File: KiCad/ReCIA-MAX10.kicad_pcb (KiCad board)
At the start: 4 copper layers, 17.4 x 51.4 mm, 9 parts, among them U1 AMS1117-3.3, U2 10M02SCU169, U5 8520_DIP

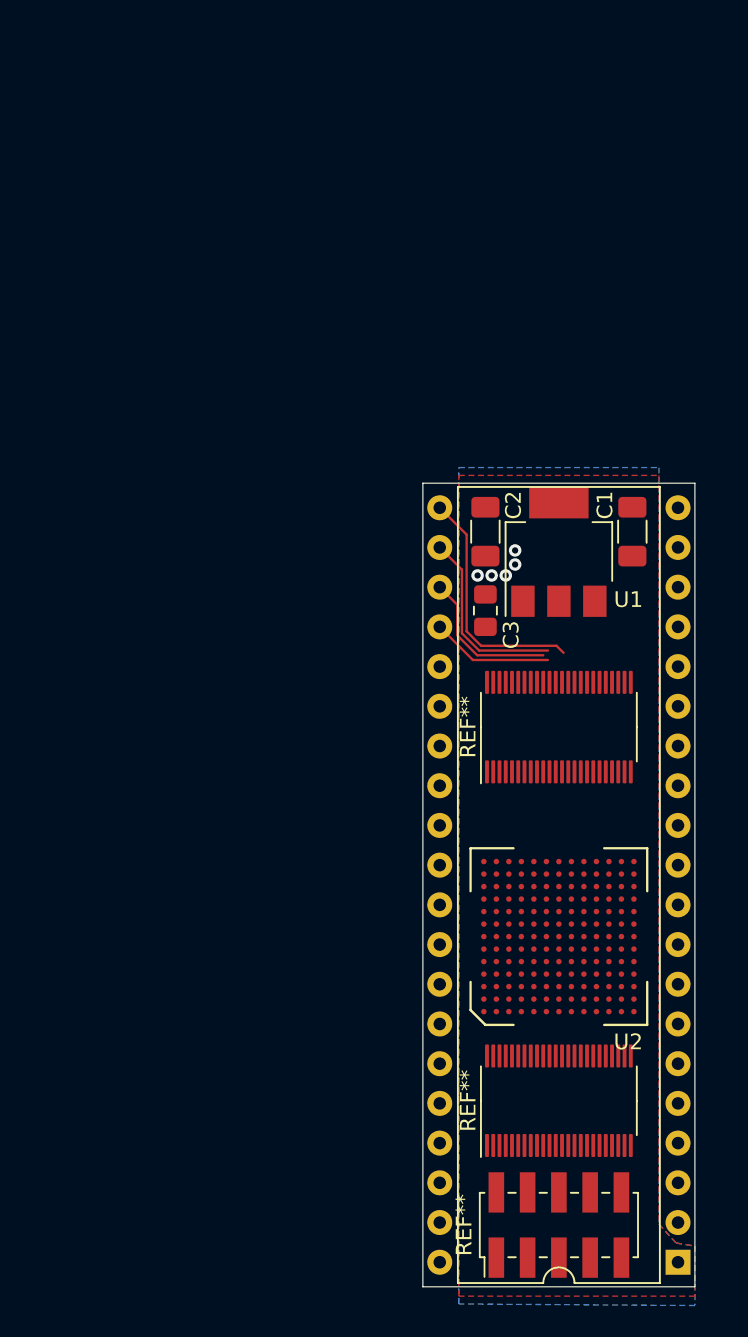
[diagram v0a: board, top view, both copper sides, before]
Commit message: Add FET bus-switch level shifters SN74CBT16210
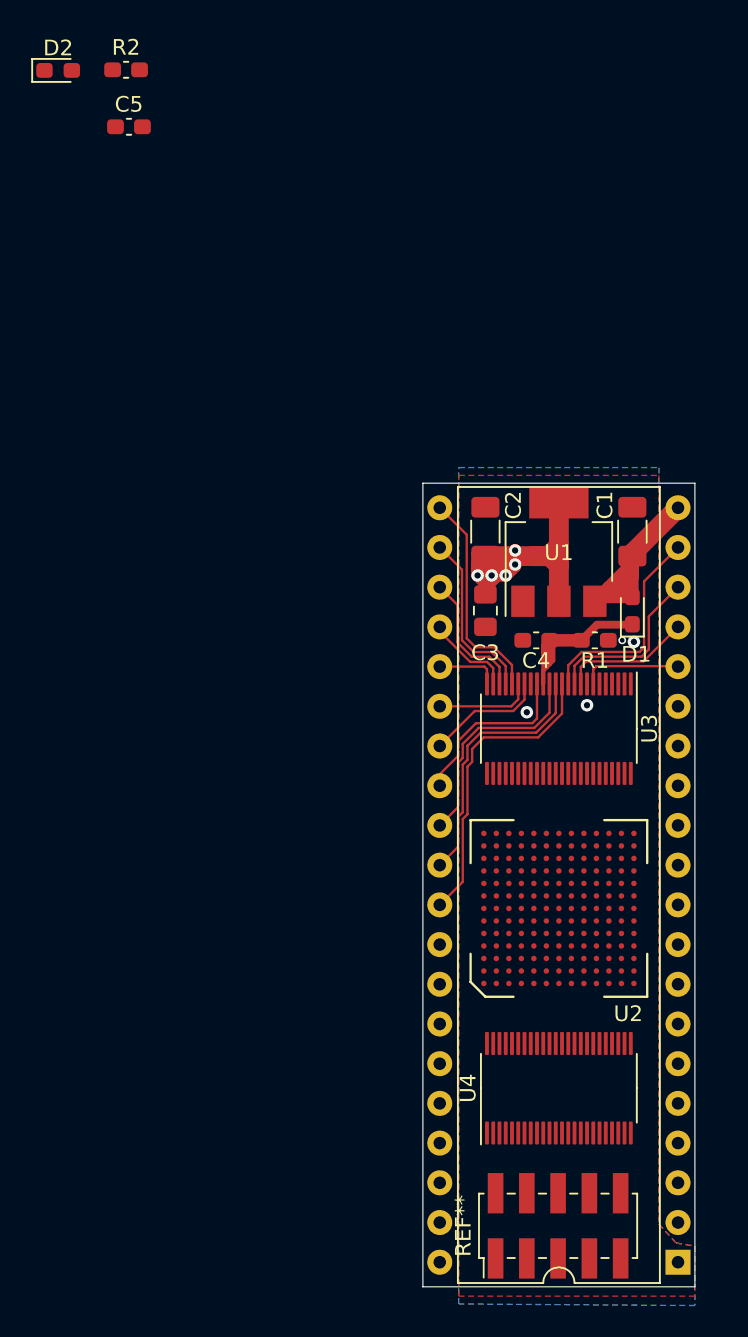
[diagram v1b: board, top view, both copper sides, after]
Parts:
- removed the REF** at (132.0, 96.8)
- removed the REF** at (132.0, 72.9)
- added C4: 0.1uF, Capacitor_SMD:C_0603_1608Metric_Pad1.08x0.95mm_HandSolder, F.Cu at (130.6, 67.3)
- added C5: 0.1uF, Capacitor_SMD:C_0603_1608Metric_Pad1.08x0.95mm_HandSolder, F.Cu at (104.5, 34.5)
- added D1: D_Small, Diode_SMD:D_0603_1608Metric_Pad1.05x0.95mm_HandSolder, F.Cu at (136.7, 65.5)
- added D2: D_Small, Diode_SMD:D_0603_1608Metric_Pad1.05x0.95mm_HandSolder, F.Cu at (100.0, 30.9)
- added R1: 2.9k, Capacitor_SMD:C_0603_1608Metric_Pad1.08x0.95mm_HandSolder, F.Cu at (134.3, 67.3)
- added R2: 2.9k, Capacitor_SMD:C_0603_1608Metric_Pad1.08x0.95mm_HandSolder, F.Cu at (104.3, 30.9)
- added U3: SN74CBT16210, Package_SO:TSSOP-48_4.4x9.7mm_P0.4mm, F.Cu at (132.0, 73.0)
- added U4: SN74CBT16210, Package_SO:TSSOP-48_4.4x9.7mm_P0.4mm, F.Cu at (132.0, 96.0)
- U5: value 8520_DIP -> 8520_DIP_SOCKET
- moved U2 1.80 mm to (132.0, 84.5)
- moved REF** 0.07 mm to (131.9, 104.8)
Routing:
- net 3V3: track 0.00 -> 33.3 mm
- net D2: track 0.00 -> 19.4 mm
- net D3: track 0.00 -> 16.7 mm
- net /4V3_U3: track 0.00 -> 16.7 mm
- net VCC: track 0.00 -> 16.4 mm
- net D4: track 0.00 -> 14.0 mm
- net TOD: track 0.00 -> 13.8 mm
- net D5: track 0.00 -> 11.2 mm
- net PC: track 0.00 -> 11.1 mm
- net PB7: track 0.00 -> 8.37 mm
- net D6: track 0.00 -> 7.66 mm
- net PB6: track 0.00 -> 6.45 mm
- net D7: track 0.00 -> 6.19 mm
- net E-CLK: track 0.00 -> 4.03 mm
- net FLAG: track 7.79 -> 5.69 mm
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
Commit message: Add JTAG-header
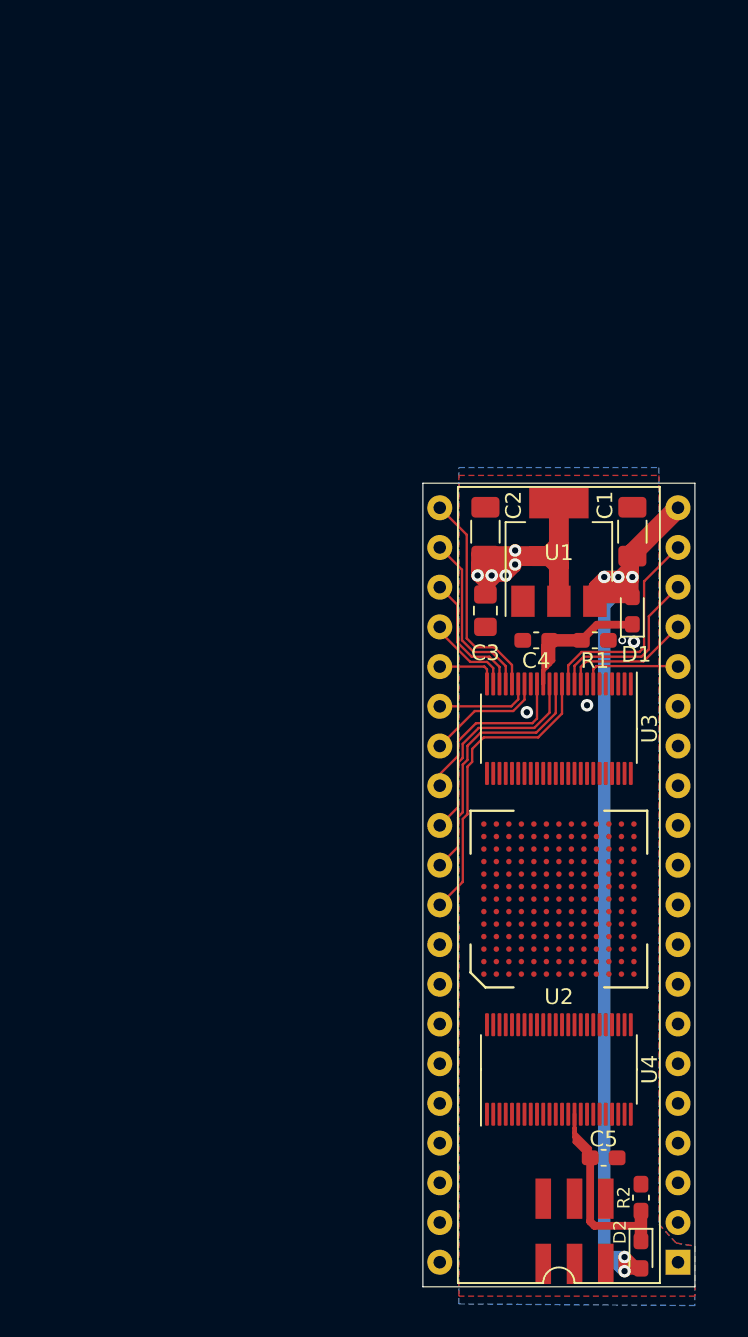
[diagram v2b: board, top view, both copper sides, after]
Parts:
- removed REF**: PinHeader_2x05_P2.00mm_Vertical_SMD, Connector_PinHeader_2.00mm:PinHeader_2x05_P2.00mm_Vertical_SMD
- added J1: Conn_02x03_Odd_Even, Connector_PinHeader_2.00mm:PinHeader_2x03_P2.00mm_Vertical_SMD, F.Cu at (133.0, 105.2)
- moved D2 84.4 mm to (137.2, 106.7), turned to 270 degrees
- moved R2 79.3 mm to (137.2, 103.0), turned to 90 degrees
- moved C5 72.6 mm to (134.9, 100.5)
- moved U4 1.20 mm to (132.0, 94.8)
- moved U2 0.60 mm to (132.0, 83.9)
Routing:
- net VCC: track 16.4 -> 75.6 mm, vias 0 -> 6
- net /4V3_U3: track 16.7 -> 33.8 mm
- net GND: track 0.00 -> 0.27 mm, vias 4 -> 3

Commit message: more routing and pin assignment
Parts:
- turned U4 to 180 degrees
- renumbered U3 to U2, U4 to U3, U2 to U4
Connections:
- net D2_3V3 renamed PB0_3V3
- C4 pad 1: /4V3_U3 -> /4V3_U2
- D1 pad 1: /4V3_U3 -> /4V3_U2
- R1 pad 1: /4V3_U3 -> /4V3_U2
- U2 pad 10: PC -> PB2
- U2 pad 11: TOD -> PB1
- U2 pad 12: D2 -> PB0
- U2 pad 15: /4V3_U3 -> /4V3_U2
- U2 pad 2: PB1 -> PB6
- U2 pad 3: PB2 -> PB7
- U2 pad 37: TOD_3V3 -> PB1_3V3
- U2 pad 38: PC_3V3 -> PB2_3V3
- U2 pad 39: PB7_3V3 -> PB3_3V3
- U2 pad 4: PB3 -> PC
- U2 pad 40: PB6_3V3 -> PB4_3V3
- U2 pad 43: PB4_3V3 -> TOD_3V3
- U2 pad 44: PB3_3V3 -> PC_3V3
- U2 pad 45: PB2_3V3 -> PB7_3V3
- U2 pad 46: PB1_3V3 -> PB6_3V3
- U2 pad 5: PB4 -> TOD
- U2 pad 7: PB6 -> PB4
- U2 pad 9: PB7 -> PB3
- U3 pad 16: Net-(U4-Pad16) -> PA7
- U3 pad 17: Net-(U4-Pad17) -> GND
- U3 pad 18: Net-(U4-Pad18) -> PA6
- U3 pad 19: Net-(U4-Pad19) -> PA5
- U3 pad 20: Net-(U4-Pad20) -> PA4
- U3 pad 21: Net-(U4-Pad21) -> PA3
- U3 pad 22: Net-(U4-Pad22) -> PA0
- U3 pad 23: Net-(U4-Pad23) -> PA1
- U3 pad 24: Net-(U4-Pad24) -> PA2
- U3 pad 32: Net-(U4-Pad32) -> GND
- U3 pad 41: Net-(U4-Pad41) -> GND
- U3 pad 8: Net-(U4-Pad8) -> GND
- U4 pad E10: 3V3 -> Net-(U4-PadE10)
- U4 pad E13: Net-(U2-PadE13) -> GND
- U4 pad F13: Net-(U2-PadF13) -> E-CLK_3V3
- U4 pad K13: Net-(U2-PadK13) -> FLAG_3V3
- U4 pad L13: Net-(U2-PadL13) -> CS_3V3
- U4 pad M13: Net-(U2-PadM13) -> RW_3V3
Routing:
- net D2: track 19.4 -> 0.00 mm
- net PB0: track 0.00 -> 18.6 mm
- net /4V3_U3: track 33.8 -> 15.9 mm
- net /4V3_U2: track 0.00 -> 16.7 mm
- net PB1: track 0.00 -> 15.8 mm
- net GND: track 0.27 -> 14.7 mm, vias 3 -> 28
- net PA7: track 0.00 -> 14.1 mm
- net PB2: track 0.00 -> 13.1 mm
- net PA6: track 0.00 -> 10.6 mm
- net PB3: track 0.00 -> 10.4 mm
- net E-CLK_3V3: track 0.00 -> 10.0 mm
- net PA0: track 0.00 -> 8.51 mm
- net PA5: track 0.00 -> 8.01 mm
- net PB4: track 0.00 -> 7.66 mm
- net FLAG_3V3: track 0.00 -> 6.76 mm
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
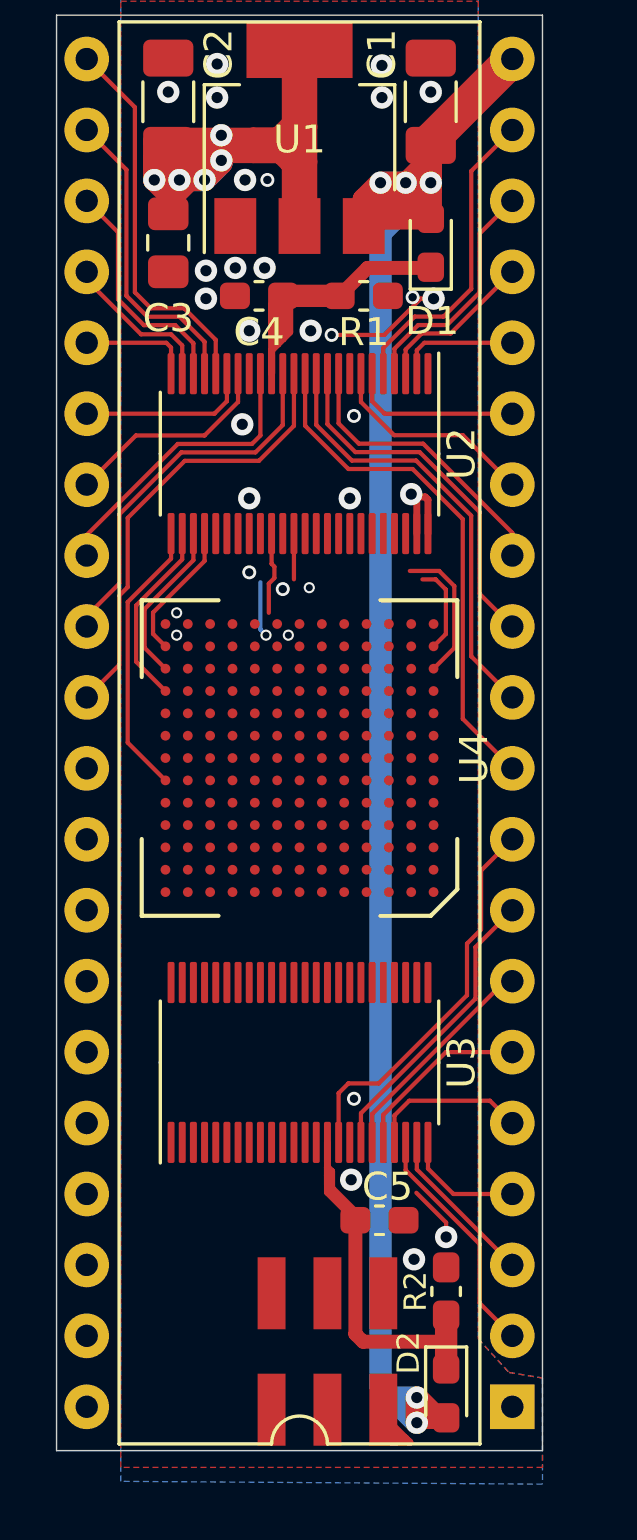
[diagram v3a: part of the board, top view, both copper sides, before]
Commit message: more routing and pin assignment
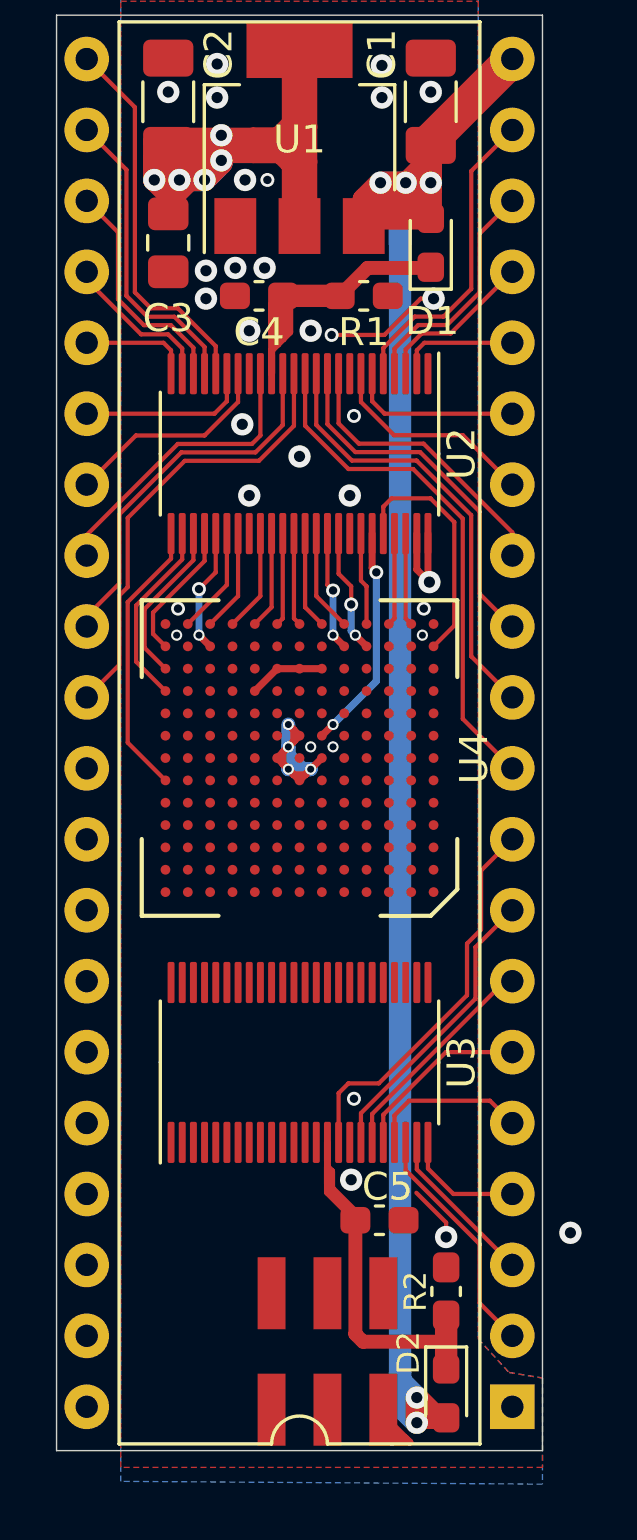
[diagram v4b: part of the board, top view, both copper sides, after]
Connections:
- U4 pad H6: Net-(U4-PadH6) -> TOD_3V3
- U4 pad M1: Net-(U4-PadM1) -> PC_3V3
- U4 pad M11: Net-(U4-PadM11) -> IRQ_3V3
- U4 pad M4: Net-(U4-PadM4) -> PB4_3V3
- U4 pad M5: Net-(U4-PadM5) -> PB3_3V3
- U4 pad N10: Net-(U4-PadN10) -> D5_3V3
- U4 pad N11: Net-(U4-PadN11) -> D6_3V3
- U4 pad N12: Net-(U4-PadN12) -> D7_3V3
- U4 pad N2: Net-(U4-PadN2) -> PB6_3V3
- U4 pad N3: Net-(U4-PadN3) -> PB7_3V3
- U4 pad N4: Net-(U4-PadN4) -> PB5_3V3
- U4 pad N5: Net-(U4-PadN5) -> PB2_3V3
- U4 pad N6: Net-(U4-PadN6) -> PB1_3V3
- U4 pad N7: Net-(U4-PadN7) -> PB0_3V3
- U4 pad N8: Net-(U4-PadN8) -> D3_3V3
- U4 pad N9: Net-(U4-PadN9) -> D4_3V3
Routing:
- net 3V3: track 36.9 -> 50.2 mm, vias 5 -> 9
- net PC_3V3: track 0.00 -> 8.74 mm
- net TOD_3V3: track 0.00 -> 8.11 mm, vias 0 -> 2
- net Net-(U4-PadL1): track 5.08 -> 0.00 mm
- net IRQ_3V3: track 0.00 -> 4.45 mm, vias 0 -> 2
- net PB4_3V3: track 0.00 -> 4.45 mm, vias 0 -> 2
- net PB3_3V3: track 0.00 -> 4.29 mm, vias 0 -> 2
- net D7_3V3: track 0.00 -> 3.82 mm
- net D5_3V3: track 0.00 -> 3.65 mm
- net PB2_3V3: track 0.00 -> 3.65 mm
- net D6_3V3: track 0.00 -> 3.65 mm
- net PB1_3V3: track 0.00 -> 3.49 mm
- net PB7_3V3: track 0.00 -> 3.32 mm
- net D3_3V3: track 0.00 -> 3.32 mm, vias 1 -> 0
- net PB5_3V3: track 0.00 -> 3.32 mm
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
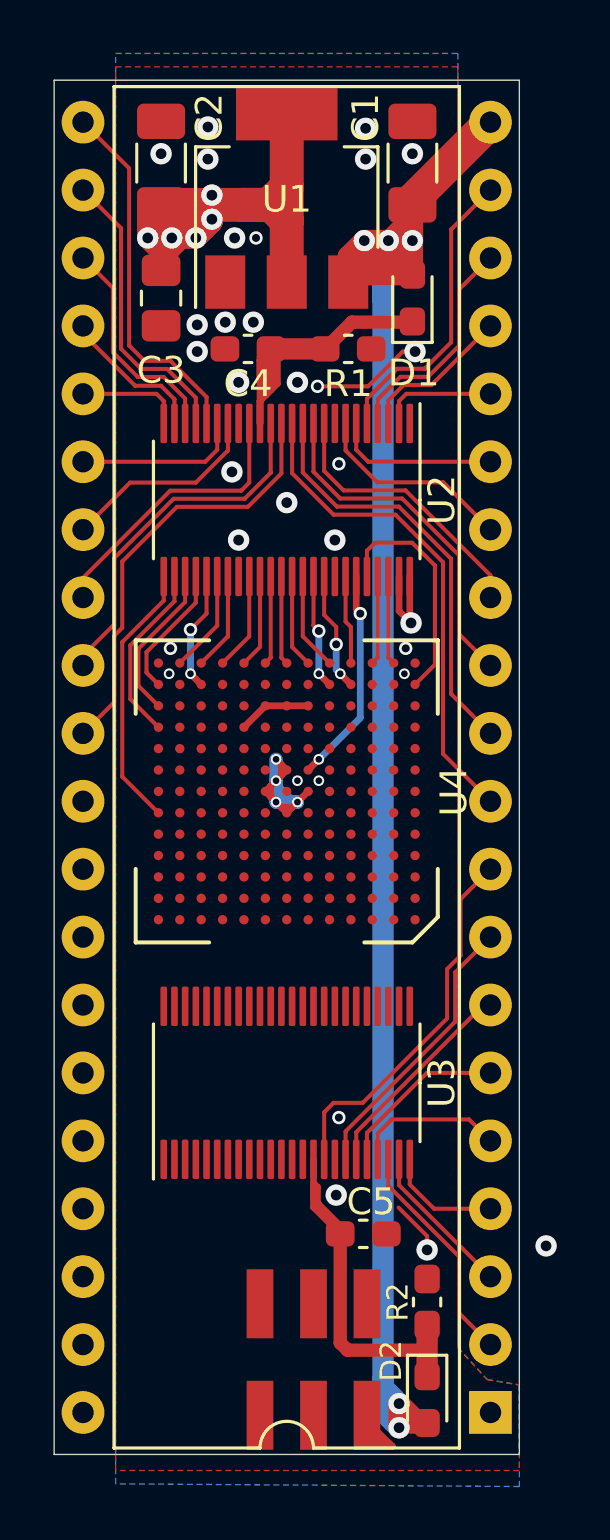
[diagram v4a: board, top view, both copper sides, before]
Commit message: routing JTAG plus more routing of power to BGA chip
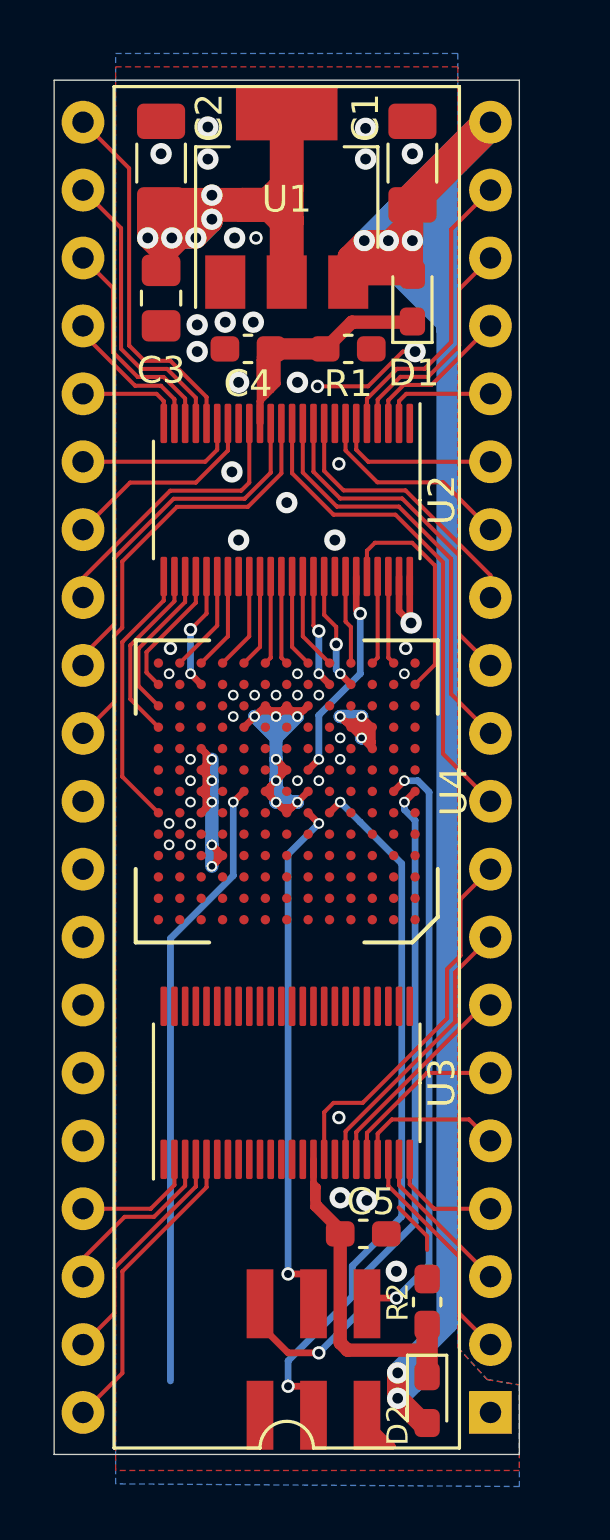
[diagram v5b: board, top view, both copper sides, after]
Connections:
- net Net-(U4-PadG9) renamed OSC_CLK
- U3 pad 2: Net-(U3-Pad2) -> A1
- U3 pad 3: Net-(U3-Pad3) -> A0
- U3 pad 4: Net-(U3-Pad4) -> SP
- U3 pad 5: Net-(U3-Pad5) -> CNT
- U4 pad G10: Net-(U4-PadG10) -> GND
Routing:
- net 3V3: track 50.2 -> 84.2 mm, vias 9 -> 20
- net TDI: track 0.00 -> 27.1 mm, vias 0 -> 2
- net TMS: track 0.00 -> 26.2 mm, vias 0 -> 2
- net OSC_CLK: track 0.00 -> 23.2 mm, vias 0 -> 1
- net TCK: track 0.00 -> 22.3 mm, vias 0 -> 2
- net TDO: track 0.00 -> 19.9 mm, vias 0 -> 2
- net VCC: track 76.2 -> 95.0 mm
- net CNT: track 0.00 -> 11.4 mm
- net SP: track 0.00 -> 8.68 mm
- net A0: track 0.00 -> 6.61 mm
- net A1: track 0.00 -> 4.75 mm
- net GND: vias 32 -> 48
